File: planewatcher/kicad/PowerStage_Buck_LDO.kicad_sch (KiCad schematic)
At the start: 25 parts, among them U12 LT8608MSE, U13 LT3045IMSE-1#PBF

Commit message: work on board layout
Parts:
- renumbered C67 to C1, C68 to C2, C69 to C3, C70 to C4, C71 to C5, C72 to C6, C73 to C7, C74 to C8, C75 to C9, L8 to L1, L9 to L2, R29 to R1, R30 to R2, R31 to R3, R32 to R4, R33 to R5, R34 to R6, R35 to R7, R36 to R8, TP17 to TP1, TP18 to TP2, TP19 to TP3, TP20 to TP4, U12 to U1, U13 to U2

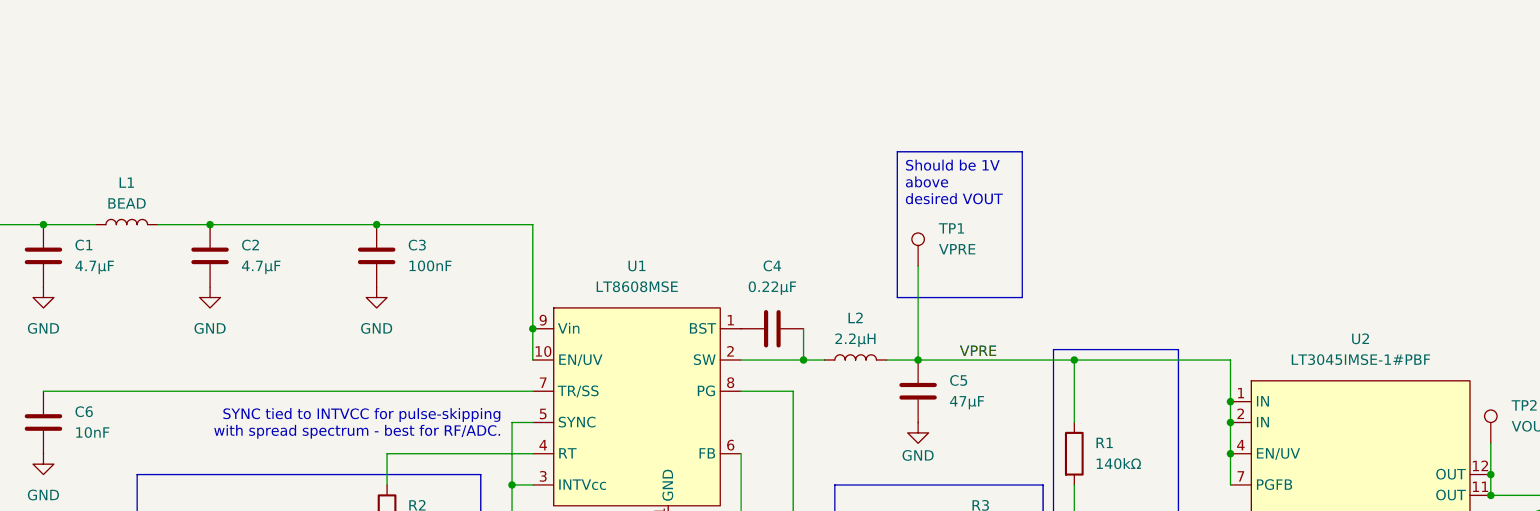
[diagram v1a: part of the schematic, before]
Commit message: address & fix ERC errors/warnings
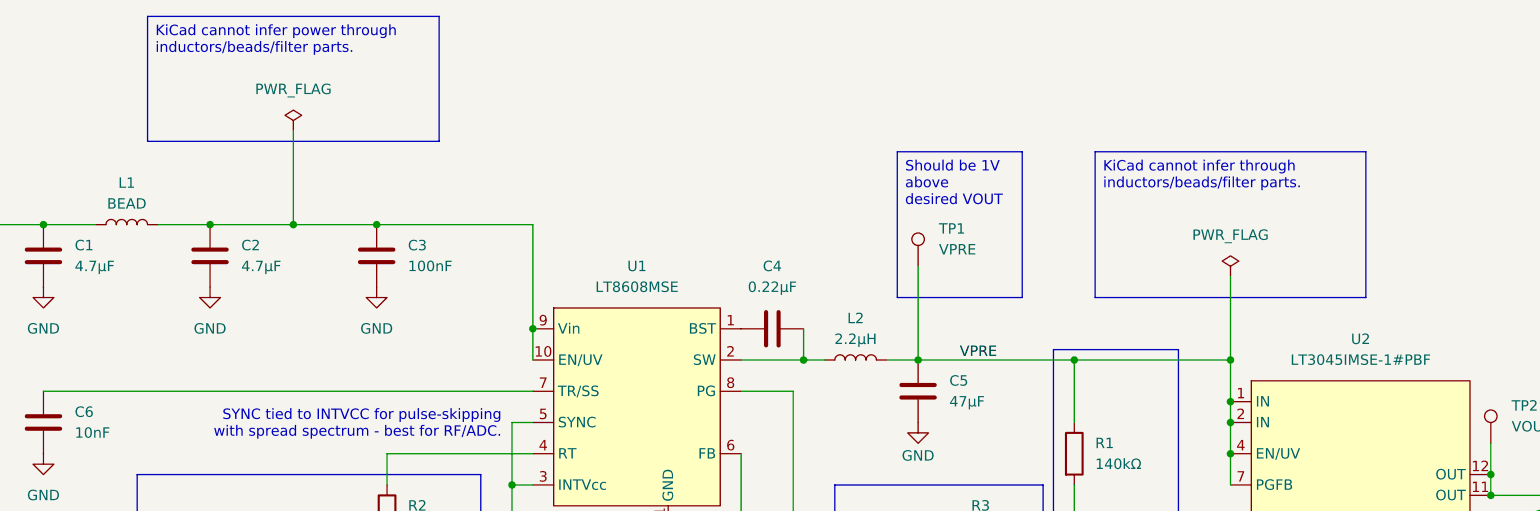
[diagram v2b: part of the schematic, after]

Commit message: updates before fab
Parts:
- C1, C2: Purpose (none) -> Input/pre-regulator ceramic capacitor for the LT8608 buck s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; Suggested Part (none) -> Murata GRM31CR71E475KA88L
- C3: Purpose (none) -> High-frequency bypass capacitor for the LT8608/LT3045 suppl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; Suggested Part (none) -> Murata GRM155R71H104KE14D
- C4: Purpose (none) -> LT8608 BST-to-SW bootstrap capacitor for the high-side swit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; Suggested Part (none) -> Murata GRM155R61H224KE01D
- C5: Purpose (none) -> LT8608 pre-regulator output bulk capacitor on VPRE.; Suggested Part (none) -> Murata GRM31CR61A476ME15L
- C6: Purpose (none) -> Soft-start or regulator control bypass capacitor in the LT8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; Suggested Part (none) -> Murata GRM155R71H103KA88D
- C7: Purpose (none) -> LT3045 output bulk capacitor for LDO stability and load tra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; Suggested Part (none) -> Samsung CL31A226KOHNNNE
- C8: Purpose (none) -> LT8608 INTVCC bypass capacitor in the low-noise pre-regulat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; Suggested Part (none) -> Murata GRM155R61C105KA12D
- C9: Purpose (none) -> LT3045 SET pin bypass/noise capacitor tied with the RSET no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; Suggested Part (none) -> TDK C1608X5R1C475K080AC
- L1: Purpose (none) -> Filters high-frequency switching noise on the low-noise reg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; Suggested Part (none) -> Murata BLM21PG600SN1D
- L2: value 2.2µH -> 4.7µH; Purpose (none) -> LT8608 buck switching inductor for the low-noise pre-regula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; Suggested Part (none) -> Coilcraft XGL4020-472MEC
- R1: Purpose (none) -> Upper resistor in the LT3045 VIOC/LT8608 feedback tracking 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; Suggested Part (none) -> Yageo RC0402FR-07140KL
- R2: Purpose (none) -> LT8608 RT resistor setting the switching frequency to appro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; Suggested Part (none) -> Yageo RC0402FR-0760K4L
- R3: Purpose (none) -> LT3045 VIOC-to-LT8608 FB tracking resistor; helps keep VPRE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; Suggested Part (none) -> Yageo RC0402FR-072K21L
- R4: Purpose (none) -> Bottom LT8608 feedback resistor in the VIOC tracking networ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; Suggested Part (none) -> Yageo RC0402FR-077K68L
- R5: Purpose (none) -> Sets the LT3045 output voltage through the 100µA SET pin re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; Suggested Part (none) -> ${RSET_Suggested_Part}
- R6: Purpose (none) -> Programs the LT3045 ILIM current limit to approximately 600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; Suggested Part (none) -> Yageo RC0402FR-07249RL
- R7: Purpose (none) -> Pull-up or bias resistor in the LT3045 power-good/control n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; Suggested Part (none) -> Yageo RC0402FR-0710KL
- R8: Purpose (none) -> LT8608 power-good pull-up or regulator status bias resistor.; Suggested Part (none) -> Yageo RC0402FR-0747KL
- TP1: Purpose (none) -> Provides oscilloscope/DMM probe access to VPRE.; Suggested Part (none) -> No fitted part (PCB pad only)
- TP2: Purpose (none) -> Provides oscilloscope/DMM probe access to VOUT.; Suggested Part (none) -> No fitted part (PCB pad only)
- TP3: Purpose (none) -> Provides oscilloscope/DMM probe access to PG_PRE.; Suggested Part (none) -> No fitted part (PCB pad only)
- TP4: Purpose (none) -> Provides oscilloscope/DMM probe access to PG_OUT.; Suggested Part (none) -> No fitted part (PCB pad only)
- U1: Purpose (none) -> Pre-regulates the protected input rail to about 1V above th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; Suggested Part (none) -> Analog Devices LT8608IMSE#PBF
- U2: Purpose (none) -> Post-regulates the buck output to the low-noise analog/RF/d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; Suggested Part (none) -> Analog Devices LT3045IMSE-1#PBF

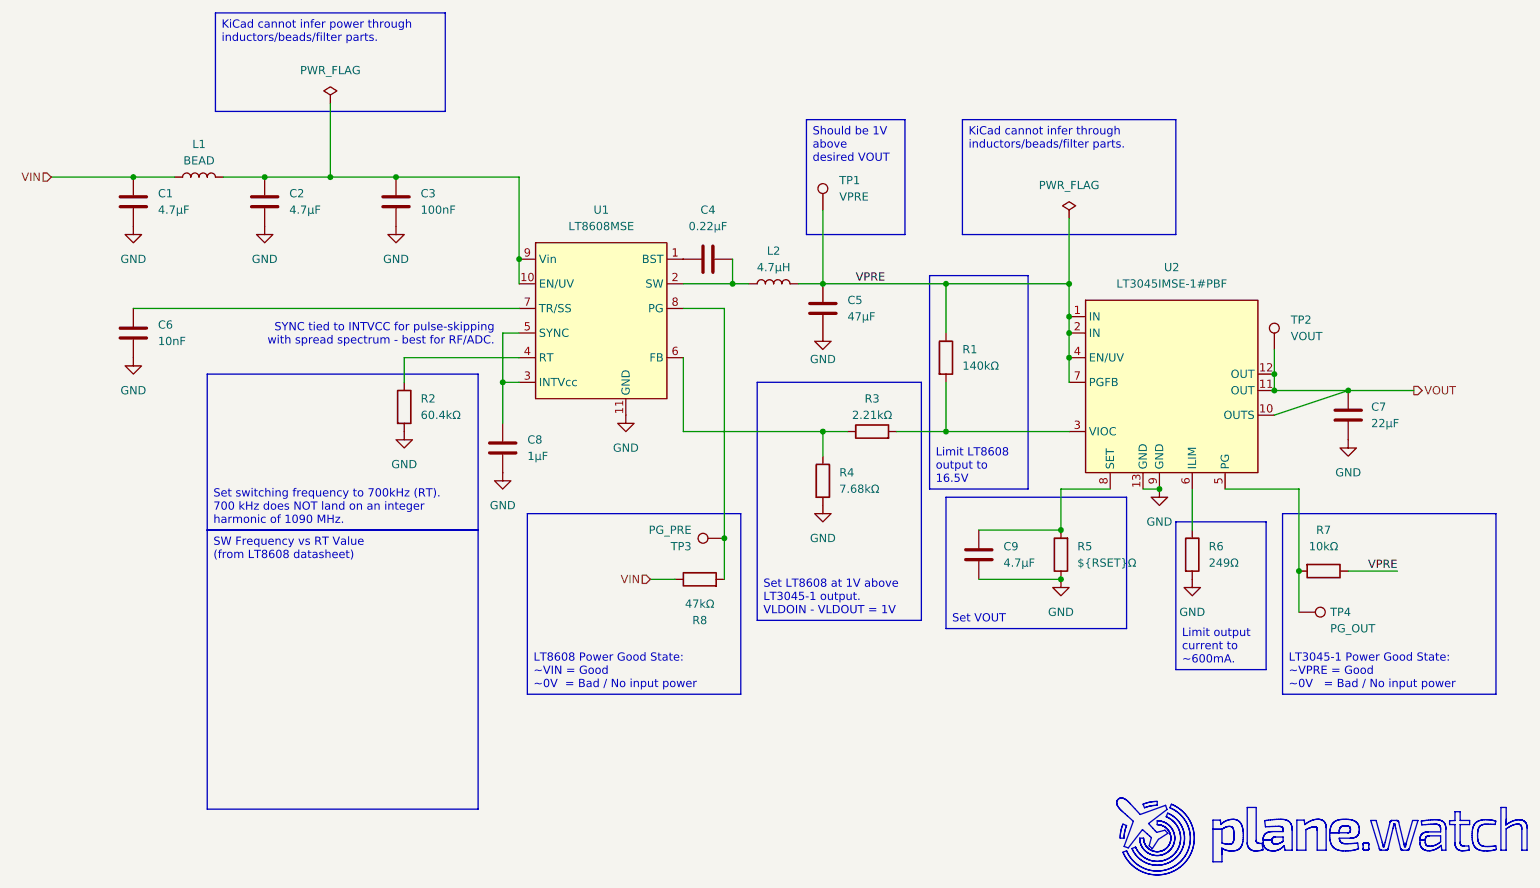
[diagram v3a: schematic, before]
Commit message: rationalise power to single 3V3 rail fed from FPGA VCC
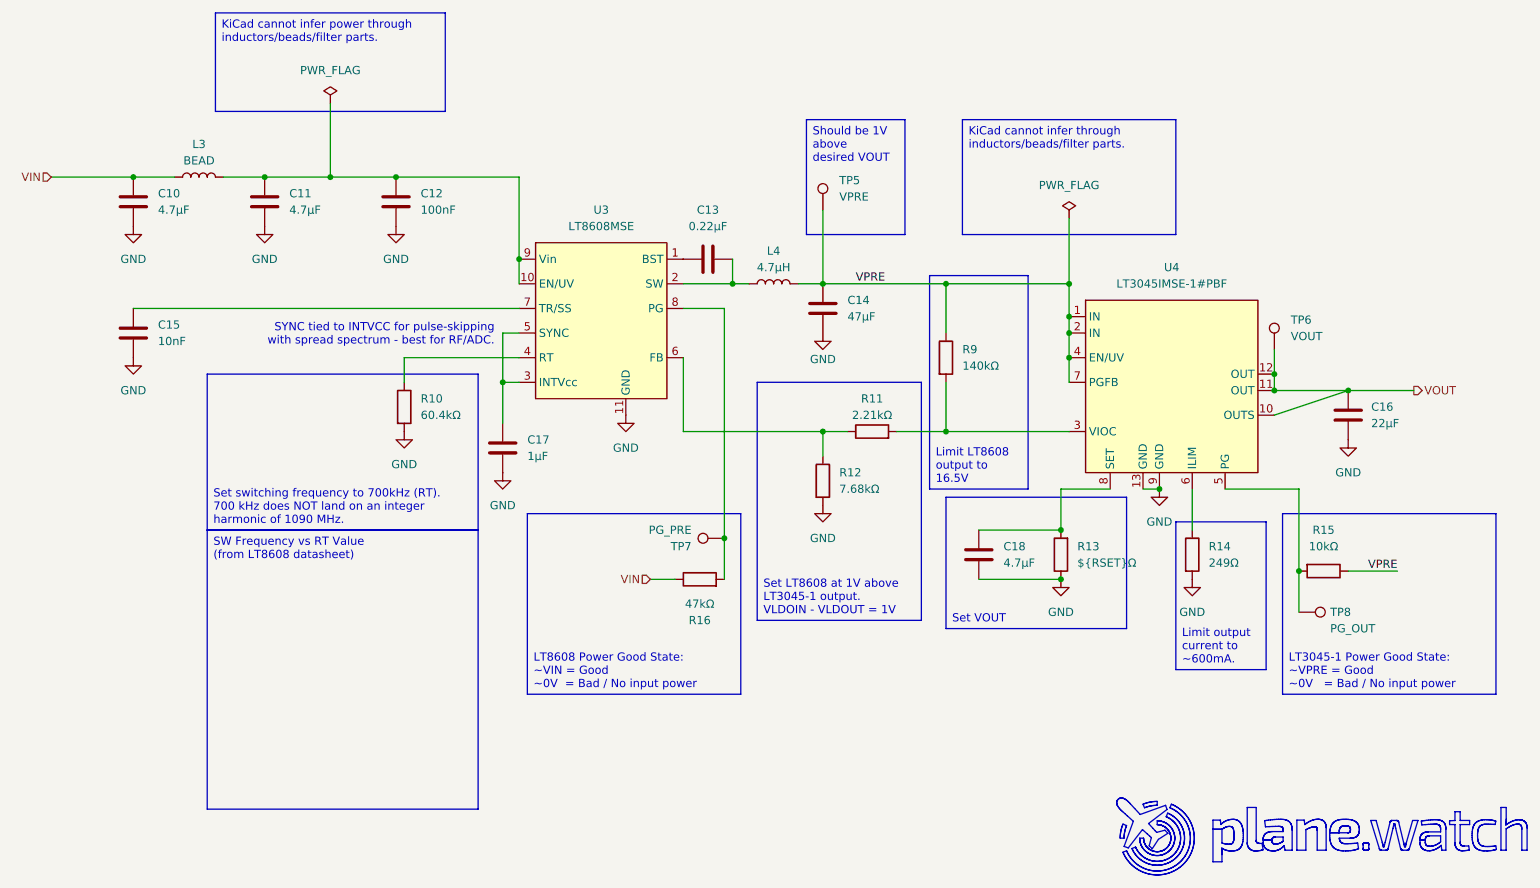
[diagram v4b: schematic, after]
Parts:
- renumbered C1 to C10, C2 to C11, C3 to C12, C4 to C13, C5 to C14, C6 to C15, C7 to C16, C8 to C17, C9 to C18, L1 to L3, L2 to L4, R2 to R10, R3 to R11, R4 to R12, R5 to R13, R6 to R14, R7 to R15, R8 to R16, R1 to R9, TP1 to TP5, TP2 to TP6, TP3 to TP7, TP4 to TP8, U1 to U3, U2 to U4

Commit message: Add persistent PCBWay BOM fields to KiCad schematic
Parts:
- C10, C11: MPN (none) -> GRM31CR71E475KA88L; Manufacturer (none) -> Murata; Package (none) -> 1206
- C12: MPN (none) -> GRM155R71H104KE14D; Manufacturer (none) -> Murata; Package (none) -> 0402
- C13: MPN (none) -> GRM155R61H224KE01D; Manufacturer (none) -> Murata; Package (none) -> 0402
- C14: MPN (none) -> GRM31CR61A476ME15L; Manufacturer (none) -> Murata; Package (none) -> 1206
- C15: MPN (none) -> GRM155R71H103KA88D; Manufacturer (none) -> Murata; Package (none) -> 0402
- C16: MPN (none) -> CL31A226KOHNNNE; Manufacturer (none) -> Samsung; Package (none) -> 1206
- C17: MPN (none) -> GRM155R61C105KA12D; Manufacturer (none) -> Murata; Package (none) -> 0402
- C18: MPN (none) -> C1608X5R1C475K080AC; Manufacturer (none) -> TDK; Package (none) -> 0603
- L3: MPN (none) -> BLM21PG600SN1D; Manufacturer (none) -> Murata; Package (none) -> 0805
- L4: MPN (none) -> XGL4020-472MEC; Manufacturer (none) -> Coilcraft; Package (none) -> XGL4020 (4x4mm)
- R10: MPN (none) -> RC0402FR-0760K4L; Manufacturer (none) -> Yageo; Package (none) -> 0402
- R11: MPN (none) -> RC0402FR-072K21L; Manufacturer (none) -> Yageo; Package (none) -> 0402
- R12: MPN (none) -> RC0402FR-077K68L; Manufacturer (none) -> Yageo; Package (none) -> 0402
- R13: MPN (none) -> ERA-2AEB303X; Manufacturer (none) -> Panasonic; Package (none) -> 0402
- R14: MPN (none) -> RC0402FR-07249RL; Manufacturer (none) -> Yageo; Package (none) -> 0402
- R15: MPN (none) -> RC0402FR-0710KL; Manufacturer (none) -> Yageo; Package (none) -> 0402
- R16: MPN (none) -> RC0402FR-0747KL; Manufacturer (none) -> Yageo; Package (none) -> 0402
- R9: MPN (none) -> RC0402FR-07140KL; Manufacturer (none) -> Yageo; Package (none) -> 0402
- U3: MPN (none) -> LT8608IMSE#PBF; Manufacturer (none) -> Analog Devices; Package (none) -> MSOP-16E
- U4: MPN (none) -> LT3045IMSE-1#PBF; Manufacturer (none) -> Analog Devices; Package (none) -> MSOP-12E

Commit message: added lcsc_ids to all parts
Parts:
- C10, C11: lcsc_id (none) -> C77094
- C12: lcsc_id (none) -> C77020
- C13: lcsc_id (none) -> C5159775
- C14: lcsc_id (none) -> C94034
- C15: lcsc_id (none) -> C77019
- C16: lcsc_id (none) -> C90146
- C17: lcsc_id (none) -> C77006
- C18: lcsc_id (none) -> C2167106
- L3: lcsc_id (none) -> C18305
- L4: lcsc_id (none) -> C6012418
- R10: lcsc_id (none) -> C327333
- R11: lcsc_id (none) -> C138019
- R12: lcsc_id (none) -> C155695
- R13: lcsc_id (none) -> C490824
- R14: lcsc_id (none) -> C185439
- R15: lcsc_id (none) -> C60490
- R16: lcsc_id (none) -> C93943
- R9: lcsc_id (none) -> C114151
- U3: lcsc_id (none) -> C580300
- U4: lcsc_id (none) -> C666588
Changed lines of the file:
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@@
 			)
 		)
+		(property "lcsc_id" "C93943"
+			(at 135.89 134.62 0)
+			(hide yes)
+			(show_name no)
+			(do_not_autoplace no)
+			(effects
+				(font
+					(size 1.27 1.27)
+				)
+			)
+		)
 		(pin "2"
 		)
@@
 			)
 		)
+		(property "lcsc_id" "C114151"
+			(at 173.99 100.33 0)
+			(hide yes)
+			(show_name no)
+			(do_not_autoplace no)
+			(effects
+				(font
+					(size 1.27 1.27)
+				)
+			)
+		)
 		(pin "1"
 		)
@@
 			)
 		)
+		(property "lcsc_id" "C666588"
+			(at 208.28 86.36 0)
+			(hide yes)
+			(show_name no)
+			(do_not_autoplace no)
+			(effects
+				(font
+					(size 1.27 1.27)
+				)
+			)
+		)
 		(pin "2"
 		)
@@
 			)
 		)
+		(property "lcsc_id" "C77020"
+			(at 88.9 76.2 0)
+			(hide yes)
+			(show_name no)
+			(do_not_autoplace no)
+			(effects
+				(font
+					(size 1.27 1.27)
+				)
+			)
+		)
 		(pin "1"
 		)
@@
 			)
 		)
+		(property "lcsc_id" "C18305"
+			(at 58.42 72.39 0)
+			(hide yes)
+			(show_name no)
+			(do_not_autoplace no)
+			(effects
+				(font
+					(size 1.27 1.27)
+				)
+			)
+		)
 		(pin "1"
 		)
@@
 			)
 		)
+		(property "lcsc_id" "C490824"
+			(at 191.77 130.81 0)
+			(hide yes)
+			(show_name no)
+			(do_not_autoplace no)
+			(effects
+				(font
+					(size 1.27 1.27)
+				)
+			)
+		)
 		(pin "1"
 		)
@@
 			)
 		)
+		(property "lcsc_id" "C77094"
+			(at 48.26 76.2 0)
+			(hide yes)
+			(show_name no)
+			(do_not_autoplace no)
+			(effects
+				(font
+					(size 1.27 1.27)
+				)
+			)
+		)
 		(pin "1"
 		)
@@
 			)
 		)
+		(property "lcsc_id" "C6012418"
+			(at 147.32 88.9 0)
+			(hide yes)
+			(show_name no)
+			(do_not_autoplace no)
+			(effects
+				(font
+					(size 1.27 1.27)
+				)
+			)
+		)
 		(pin "1"
 		)
@@
 			)
 		)
+		(property "lcsc_id" "C155695"
+			(at 154.94 119.38 0)
+			(hide yes)
+			(show_name no)
+			(do_not_autoplace no)
+			(effects
+				(font
+					(size 1.27 1.27)
+				)
+			)
+		)
 		(pin "1"
 		)
@@
 			)
 		)
+		(property "lcsc_id" "C580300"
+			(at 120.65 78.74 0)
+			(hide yes)
+			(show_name no)
+			(do_not_autoplace no)
+			(effects
+				(font
+					(size 1.27 1.27)
+				)
+			)
+		)
 		(pin "3"
 		)
@@
 			)
 		)
+		(property "lcsc_id" "C77094"
+			(at 68.58 76.2 0)
+			(hide yes)
+			(show_name no)
+			(do_not_autoplace no)
+			(effects
+				(font
+					(size 1.27 1.27)
+				)
+			)
+		)
 		(pin "1"
 		)
@@
 			)
 		)
+		(property "lcsc_id" "C77019"
+			(at 48.26 96.52 0)
+			(hide yes)
+			(show_name no)
+			(do_not_autoplace no)
+			(effects
+				(font
+					(size 1.27 1.27)
+				)
+			)
+		)
 		(pin "2"
 		)
@@
 			)
 		)
+		(property "lcsc_id" "C185439"
+			(at 212.09 130.81 0)
+			(hide yes)
+			(show_name no)
+			(do_not_autoplace no)
+			(effects
+				(font
+					(size 1.27 1.27)
+				)
+			)
+		)
 		(pin "1"
 		)
@@
 			)
 		)
+		(property "lcsc_id" "C94034"
+			(at 154.94 92.71 0)
+			(hide yes)
+			(show_name no)
+			(do_not_autoplace no)
+			(effects
+				(font
+					(size 1.27 1.27)
+				)
+			)
+		)
 		(pin "1"
 		)
@@
 			)
 		)
+		(property "lcsc_id" "C60490"
+			(at 232.41 133.35 0)
+			(hide yes)
+			(show_name no)
+			(do_not_autoplace no)
+			(effects
+				(font
+					(size 1.27 1.27)
+				)
+			)
+		)
 		(pin "2"
 		)
@@
 			)
 		)
+		(property "lcsc_id" "C5159775"
+			(at 137.16 85.09 0)
+			(hide yes)
+			(show_name no)
+			(do_not_autoplace no)
+			(effects
+				(font
+					(size 1.27 1.27)
+				)
+			)
+		)
 		(pin "1"
 		)
@@
 			)
 		)
+		(property "lcsc_id" "C138019"
+			(at 162.56 111.76 0)
+			(hide yes)
+			(show_name no)
+			(do_not_autoplace no)
+			(effects
+				(font
+					(size 1.27 1.27)
+				)
+			)
+		)
 		(pin "2"
 		)
@@
 			)
 		)
+		(property "lcsc_id" "C77006"
+			(at 105.41 114.3 0)
+			(hide yes)
+			(show_name no)
+			(do_not_autoplace no)
+			(effects
+				(font
+					(size 1.27 1.27)
+				)
+			)
+		)
 		(pin "1"
 		)
@@
 			)
 		)
+		(property "lcsc_id" "C2167106"
+			(at 179.07 130.81 0)
+			(hide yes)
+			(show_name no)
+			(do_not_autoplace no)
+			(effects
+				(font
+					(size 1.27 1.27)
+				)
+			)
+		)
 		(pin "2"
 		)
@@
 			)
 		)
+		(property "lcsc_id" "C327333"
+			(at 90.17 107.95 0)
+			(hide yes)
+			(show_name no)
+			(do_not_autoplace no)
+			(effects
+				(font
+					(size 1.27 1.27)
+				)
+			)
+		)
 		(pin "2"
 		)
@@
 			(at 236.22 109.22 0)
 			(hide yes)
+			(show_name no)
+			(do_not_autoplace no)
+			(effects
+				(font
+					(size 1.27 1.27)
+				)
+			)
+		)
+		(property "lcsc_id" "C90146"
+			(at 236.22 109.22 0)
+			(hide yes)
